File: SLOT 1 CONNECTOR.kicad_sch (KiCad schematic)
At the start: 10 parts, among them J33 Slot1, U24 MAX1617 ME

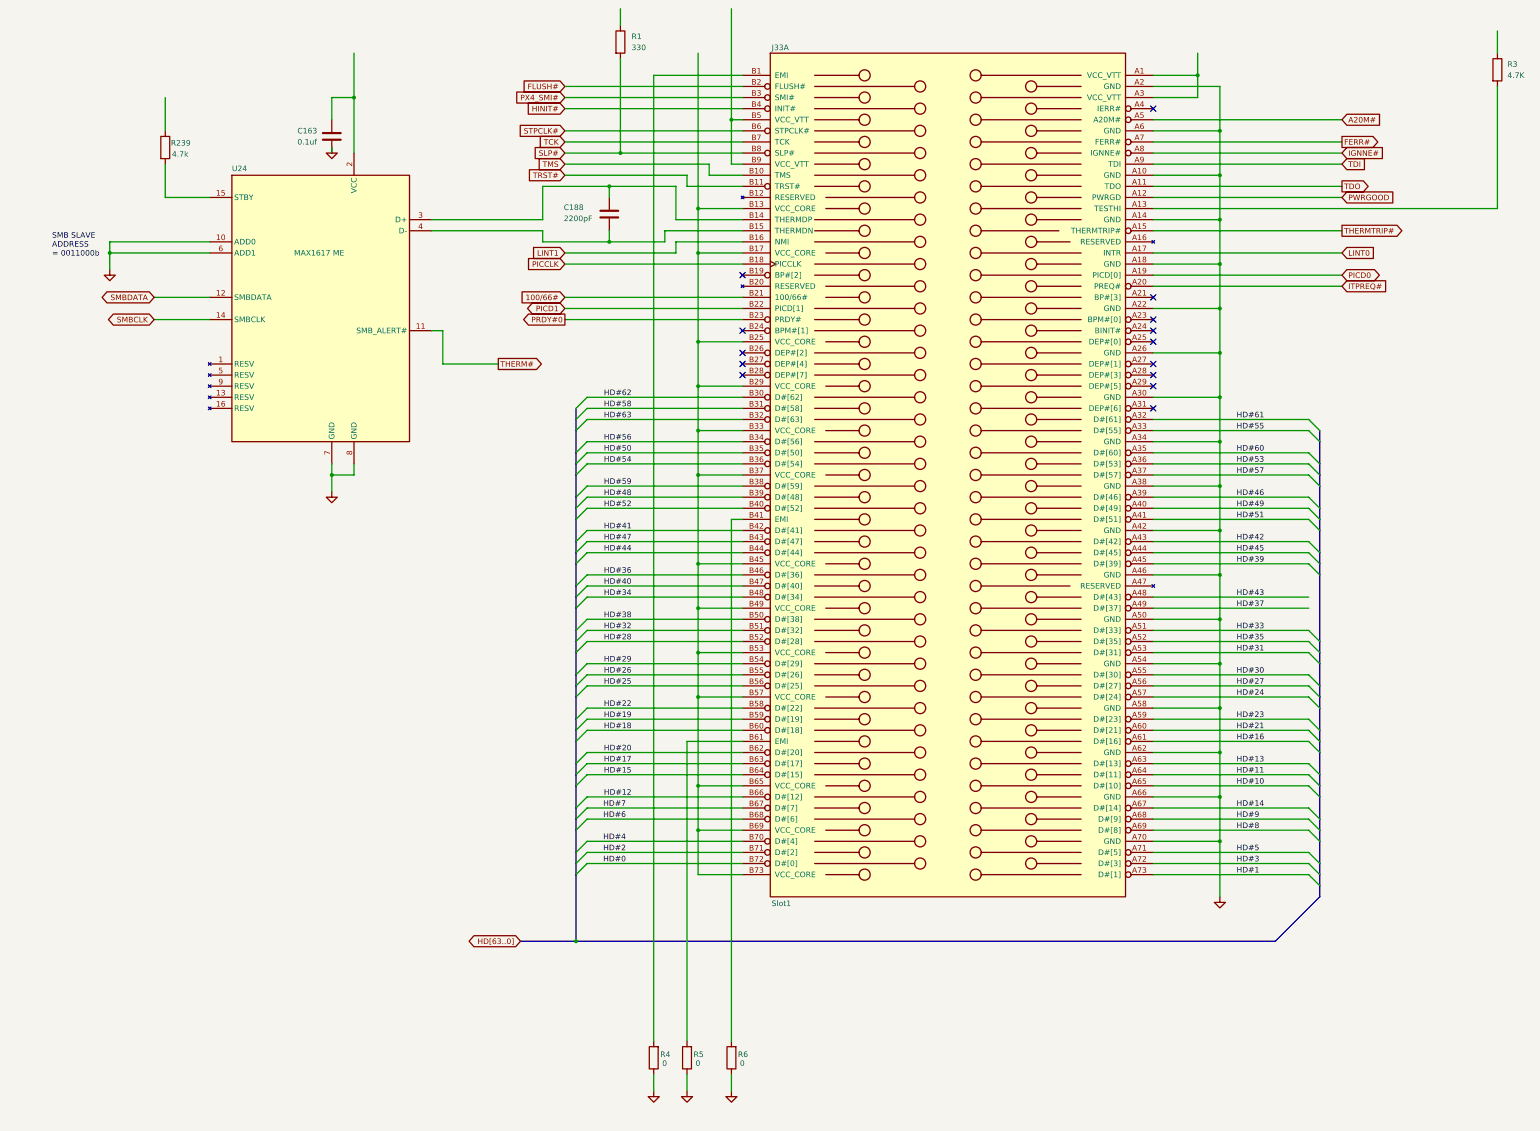
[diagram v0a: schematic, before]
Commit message: page 3 4 clickable links added
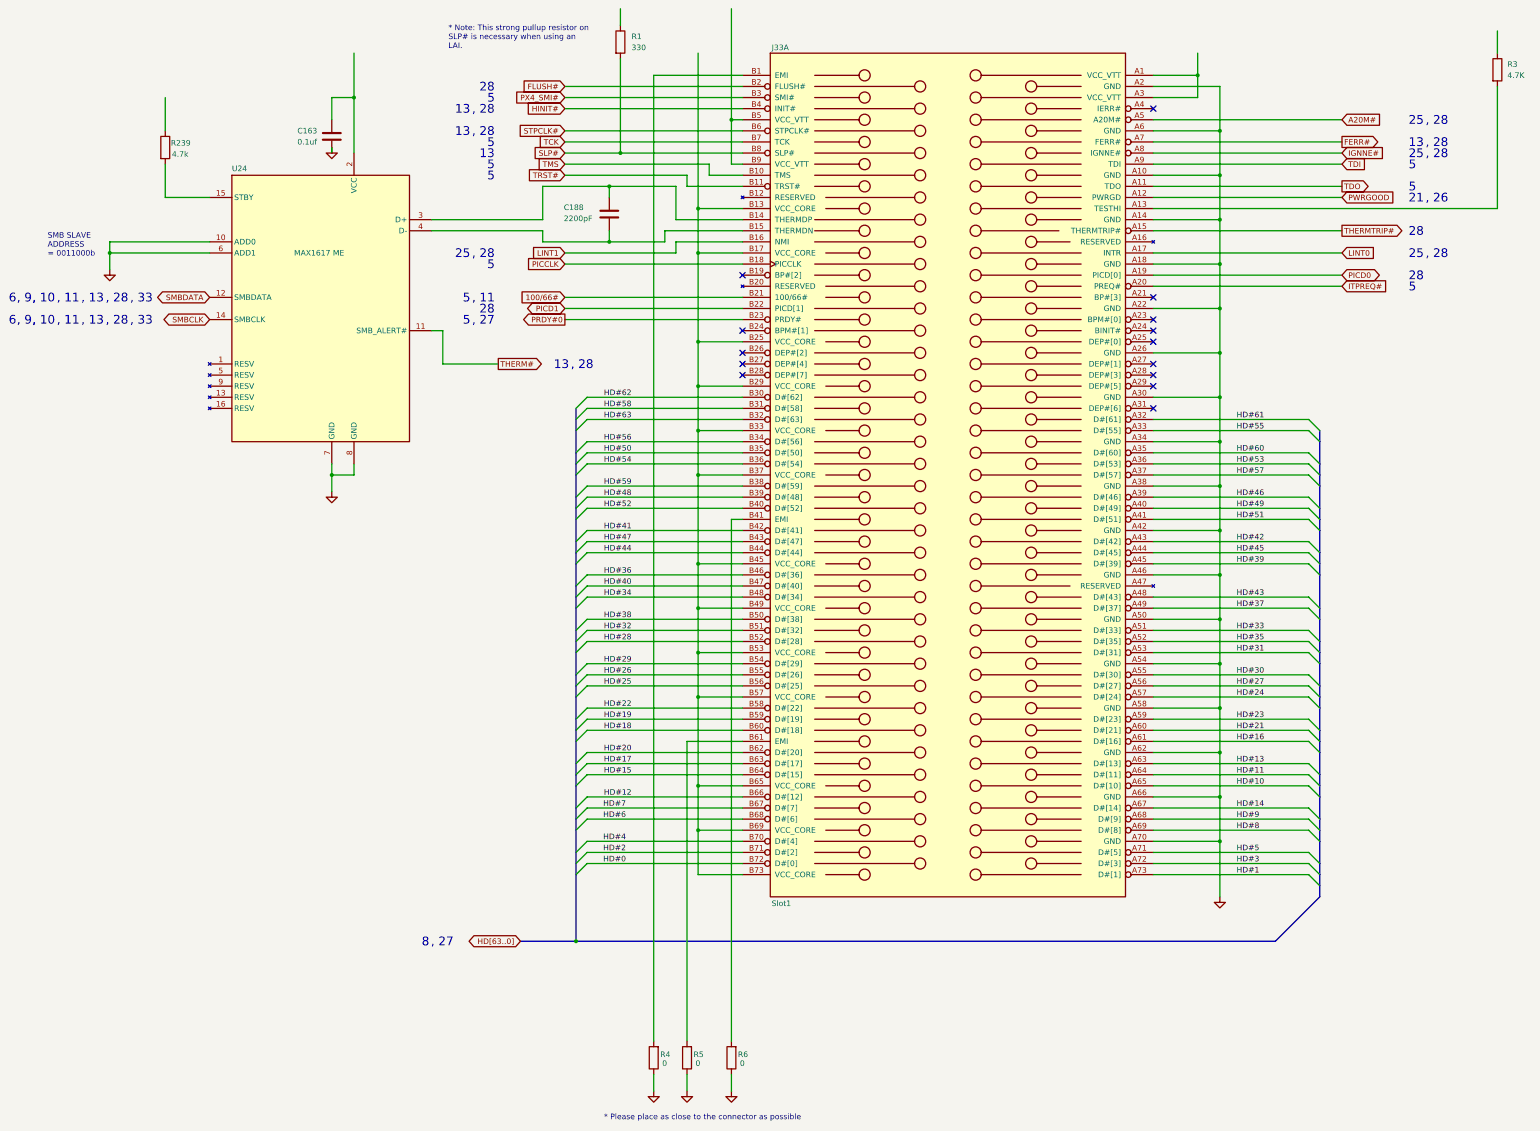
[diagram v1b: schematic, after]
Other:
- note added: "* Note: This strong pullup resistor on SLP# is necessary when using an LAI."
- note added: "* Please place as close to the connector as possible"
- note added: ","
- note added: "10"
- note added: "11"
- note added: "13"
- note added: "21"
- note added: "25"
- note added: "26"
- note added: "27"
- note added: "28"
- note added: "33"
- note added: "5"
- note added: "6"
- note added: "8"
- note added: "9"

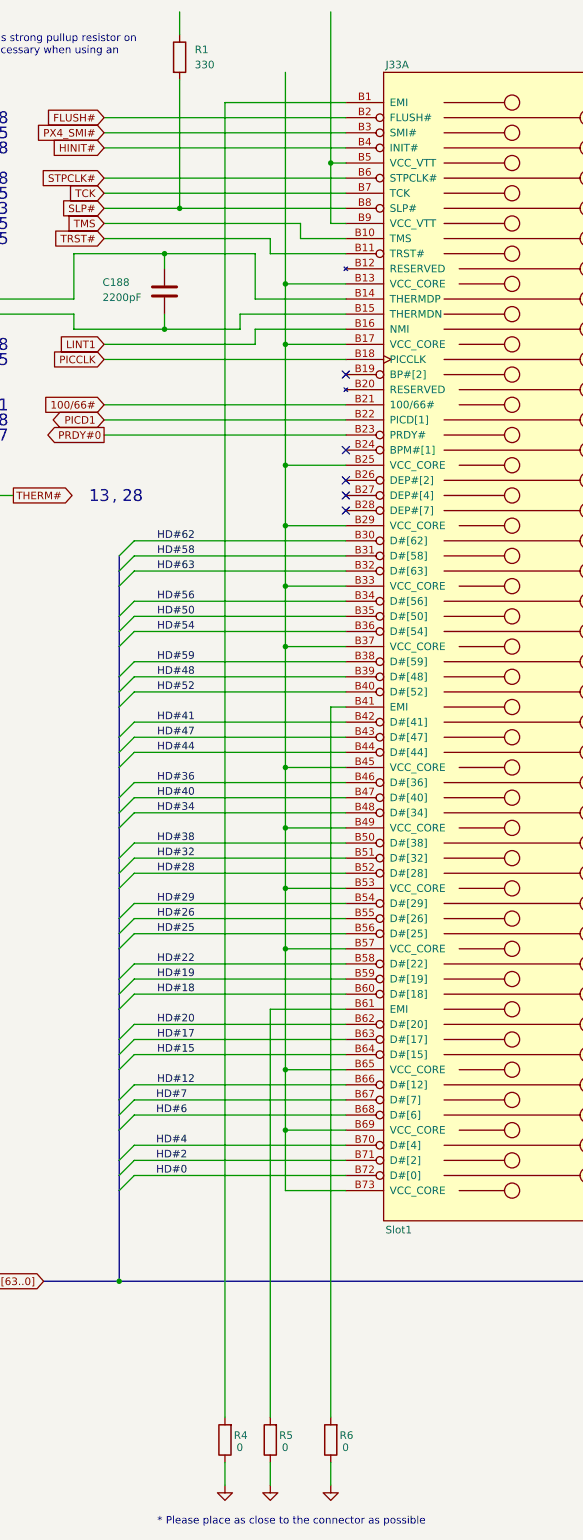
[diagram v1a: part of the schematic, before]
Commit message: pages 9 10 11 DIMM socket and DIMM socket symbol
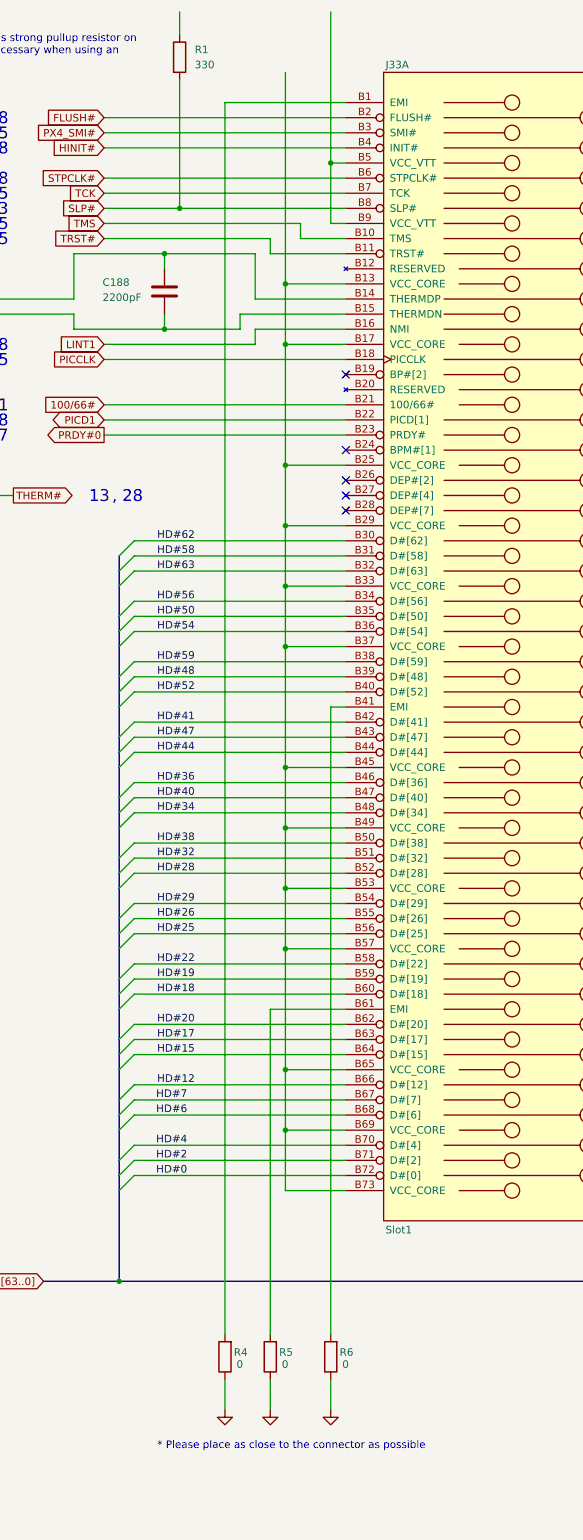
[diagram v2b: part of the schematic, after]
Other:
- moved on the sheet: R4, R5, R6

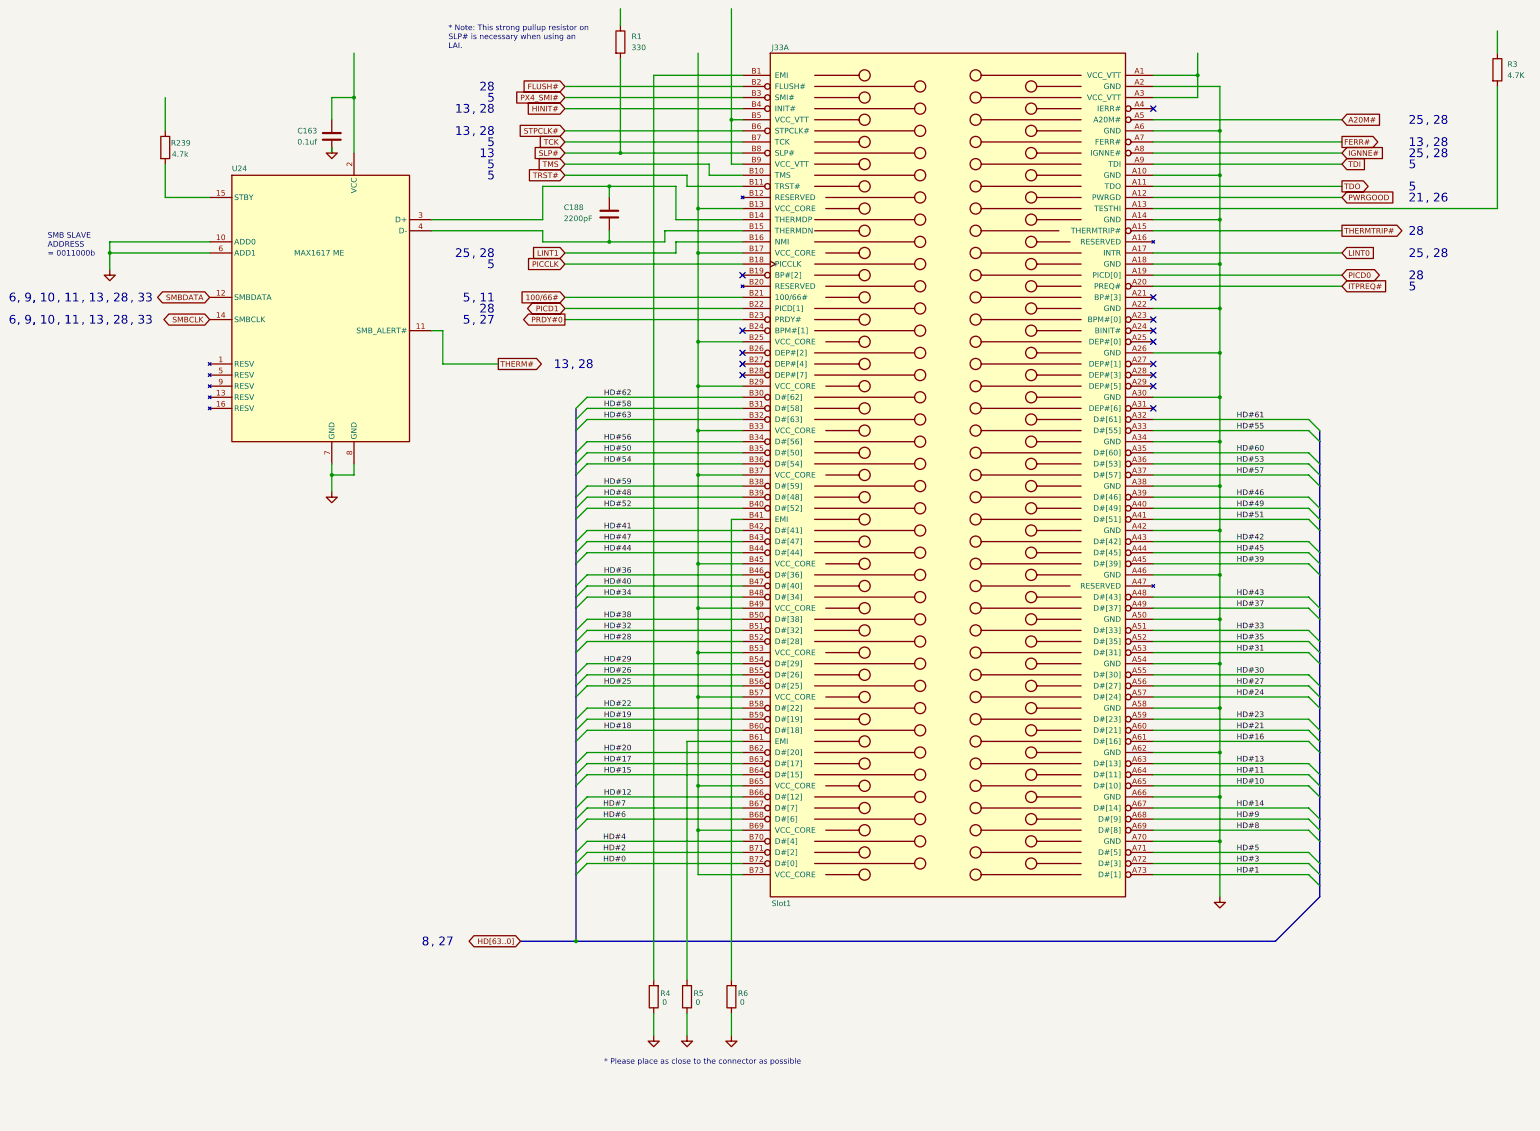
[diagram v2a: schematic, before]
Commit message: page 18 ISA, small fixes
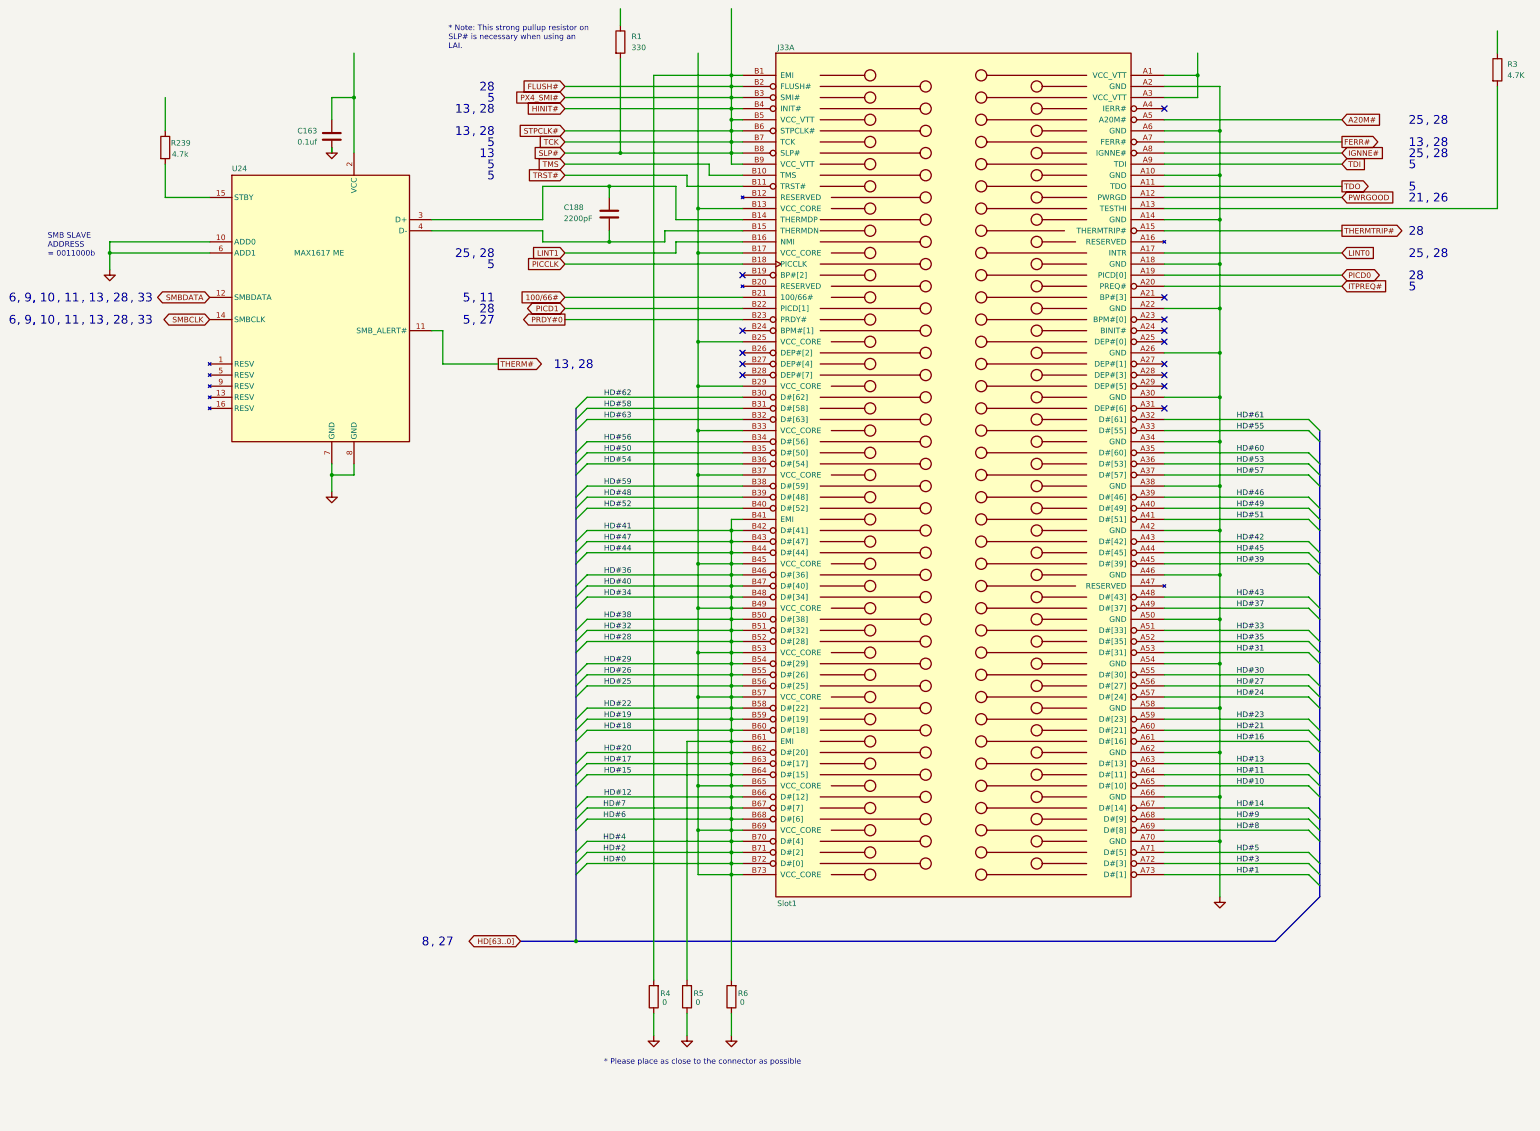
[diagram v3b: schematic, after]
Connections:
- net HD#12 is gone; now on net HD#0: J33.B66 (D#[12])
- net HD#15 is gone; now on net HD#0: J33.B64 (D#[15])
- net HD#17 is gone; now on net HD#0: J33.B63 (D#[17])
- net HD#18 is gone; now on net HD#0: J33.B60 (D#[18])
- net HD#19 is gone; now on net HD#0: J33.B59 (D#[19])
- net HD#2 is gone; now on net HD#0: J33.B71 (D#[2])
- net HD#20 is gone; now on net HD#0: J33.B62 (D#[20])
- net HD#22 is gone; now on net HD#0: J33.B58 (D#[22])
- net HD#25 is gone; now on net HD#0: J33.B56 (D#[25])
- net HD#26 is gone; now on net HD#0: J33.B55 (D#[26])
- net HD#28 is gone; now on net HD#0: J33.B52 (D#[28])
- net HD#29 is gone; now on net HD#0: J33.B54 (D#[29])
- net HD#32 is gone; now on net HD#0: J33.B51 (D#[32])
- net HD#34 is gone; now on net HD#0: J33.B48 (D#[34])
- net HD#36 is gone; now on net HD#0: J33.B46 (D#[36])
- net HD#38 is gone; now on net HD#0: J33.B50 (D#[38])
- net HD#4 is gone; now on net HD#0: J33.B70 (D#[4])
- net HD#40 is gone; now on net HD#0: J33.B47 (D#[40])
- net HD#41 is gone; now on net HD#0: J33.B42 (D#[41])
- net HD#44 is gone; now on net HD#0: J33.B44 (D#[44])
- net HD#47 is gone; now on net HD#0: J33.B43 (D#[47])
- net HD#6 is gone; now on net HD#0: J33.B68 (D#[6])
- net HD#7 is gone; now on net HD#0: J33.B67 (D#[7])
- net HINIT# is gone; now on net FLUSH#: J33.B4 (INIT#)
- net PX4_SMI# is gone; now on net FLUSH#: J33.B3 (SMI#)
- net SLP# is gone; now on net FLUSH#: J33.B8 (SLP#), R1.2
- net STPCLK# is gone; now on net FLUSH#: J33.B6 (STPCLK#)
- net TCK is gone; now on net FLUSH#: J33.B7 (TCK)
- net FLUSH#: now also J33.B1 (EMI), J33.B5 (VCC_VTT), J33.B9 (VCC_VTT), R4.2
- net HD#0: now also J33.B13 (VCC_CORE), J33.B17 (VCC_CORE), J33.B25 (VCC_CORE), J33.B29 (VCC_CORE), J33.B33 (VCC_CORE), J33.B37 (VCC_CORE), J33.B41 (EMI), J33.B45 (VCC_CORE), J33.B49 (VCC_CORE), J33.B53 (VCC_CORE), J33.B57 (VCC_CORE), J33.B61 (EMI), J33.B65 (VCC_CORE), J33.B69 (VCC_CORE), J33.B73 (VCC_CORE), R5.2, R6.2
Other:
- moved on the sheet: J33A
